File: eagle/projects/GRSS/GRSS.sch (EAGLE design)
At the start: 24 parts, among them J1 MOL-SL-2-RA, J10 MOL-SL-2-RA, J11 M02PTH, J2 MOL-SL-2-RA, J3 MOL-SL-2-RA, J4 MOL-SL-2-RA, J5 MOL-SL-2-RA, J6 MOL-SL-2-RA, J7 MOL-SL-2-RA, J8 MOL-SL-2-RA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

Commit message: modified 555 Timer -> T=~3s
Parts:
- R4: value 76.8k -> 240k; device grss:RES_76R8_0603 -> grss:RES_240R0_0603
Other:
- note added: "555 Timer - ~3s"
- note removed: "555 Timer - ~1Hz"
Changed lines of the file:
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@@
 <part name="R2" library="grss" deviceset="RES" device="_0603" technology="_100R" value="100"/>
 <part name="R3" library="grss" deviceset="RES" device="_0603" technology="_100R" value="100"/>
-<part name="R4" library="grss" deviceset="RES" device="_0603" technology="_76R8" value="76.8k"/>
+<part name="R4" library="grss" deviceset="RES" device="_0603" technology="_240R0" value="240k"/>
 <part name="C1" library="grss" deviceset="CAP" device="_0603" technology="_100NF0" value="100nF"/>
 <part name="C2" library="grss" deviceset="CAP" device="_0603" technology="_10UF0" value="10uF"/>
@@
 <sheet>
 <plain>
-<text x="65.786" y="90.17" size="2.54" layer="91">TITLE_TOC</text>
-<text x="65.786" y="85.09" size="2.54" layer="91">BLOCK_DIAGRAM</text>
-<text x="65.786" y="80.01" size="2.54" layer="91">SCHEMATIC</text>
-<text x="22.86" y="154.94" size="6.4516" layer="91">Global Recovery Signalling System (GRSS)</text>
-<text x="191.262" y="12.7" size="2.54" layer="91">TITLE_TOC</text>
+<text x="65.786" y="90.17" size="2.54" layer="95">TITLE_TOC</text>
+<text x="65.786" y="85.09" size="2.54" layer="95">BLOCK_DIAGRAM</text>
+<text x="65.786" y="80.01" size="2.54" layer="95">SCHEMATIC</text>
+<text x="22.86" y="154.94" size="6.4516" layer="95">Global Recovery Signalling System (GRSS)</text>
+<text x="191.262" y="12.7" size="2.54" layer="95">TITLE_TOC</text>
 </plain>
 <instances>
@@
 <sheet>
 <plain>
-<text x="-50.8" y="177.8" size="1.778" layer="91">LED1</text>
-<text x="-50.8" y="157.48" size="1.778" layer="91">LED2</text>
-<text x="-50.8" y="137.16" size="1.778" layer="91">LED3</text>
-<text x="-22.86" y="177.8" size="1.778" layer="91">LED4</text>
-<text x="-22.86" y="157.48" size="1.778" layer="91">LED5</text>
-<text x="-22.86" y="137.16" size="1.778" layer="91">LED6</text>
-<text x="5.08" y="177.8" size="1.778" layer="91">LED7</text>
-<text x="5.08" y="157.48" size="1.778" layer="91">LED8</text>
-<text x="5.08" y="137.16" size="1.778" layer="91">LED9</text>
-<text x="33.02" y="157.48" size="1.778" layer="91">Buzzer</text>
-<text x="-124.46" y="129.54" size="1.778" layer="91">555 Timer - ~1Hz</text>
-<text x="-129.54" y="170.18" size="1.778" layer="91">LDO 9V -&gt; 4.5V</text>
-<text x="21.59" y="68.58" size="2.54" layer="91">SCHEMATIC</text>
+<text x="-50.8" y="177.8" size="1.778" layer="97">LED1</text>
+<text x="-50.8" y="157.48" size="1.778" layer="97">LED2</text>
+<text x="-50.8" y="137.16" size="1.778" layer="97">LED3</text>
+<text x="-22.86" y="177.8" size="1.778" layer="97">LED4</text>
+<text x="-22.86" y="157.48" size="1.778" layer="97">LED5</text>
+<text x="-22.86" y="137.16" size="1.778" layer="97">LED6</text>
+<text x="5.08" y="177.8" size="1.778" layer="97">LED7</text>
+<text x="5.08" y="157.48" size="1.778" layer="97">LED8</text>
+<text x="5.08" y="137.16" size="1.778" layer="97">LED9</text>
+<text x="33.02" y="157.48" size="1.778" layer="97">Buzzer</text>
+<text x="-124.46" y="129.54" size="1.778" layer="97">555 Timer - ~3s</text>
+<text x="-129.54" y="170.18" size="1.778" layer="97">LDO 9V -&gt; 4.5V</text>
+<text x="21.59" y="68.58" size="2.54" layer="95">SCHEMATIC</text>
 </plain>
 <instances>

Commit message: Added NC (no connect) to lib and sch
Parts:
- added NC1: NC, grss:NO_CONNECT
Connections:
- new net N$1: NC1.NC, U2.CVOLT
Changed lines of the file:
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@@
 <part name="FRAME2" library="frames" deviceset="A4L-LOC" device=""/>
 <part name="U$1" library="grss" deviceset="TOC" device="" value="TOC"/>
+<part name="NC1" library="grss" deviceset="NO_CONNECT" device="" value="NC"/>
 </parts>
 <sheets>
@@
 <instance part="J9" gate="G$1" x="17.78" y="137.16"/>
 <instance part="J10" gate="G$1" x="45.72" y="157.48"/>
+<instance part="NC1" gate="G$1" x="-78.74" y="127" rot="R180"/>
 </instances>
 <busses>
@@
 </segment>
 </net>
+<net name="N$1" class="0">
+<segment>
+<pinref part="U2" gate="A" pin="CVOLT"/>
+<pinref part="NC1" gate="G$1" pin="NC"/>
+<wire x1="-78.74" y1="127" x2="-83.82" y2="127" width="0.1524" layer="91"/>
+</segment>
+</net>

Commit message: Package updates for component check / added block diagram sheet
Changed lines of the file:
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@@
 <layers>
 <layer number="1" name="Top" color="4" fill="1" visible="no" active="no"/>
+<layer number="2" name="Route2" color="1" fill="3" visible="no" active="no"/>
+<layer number="3" name="Route3" color="4" fill="3" visible="no" active="no"/>
+<layer number="14" name="Route14" color="1" fill="6" visible="no" active="no"/>
+<layer number="15" name="Route15" color="4" fill="6" visible="no" active="no"/>
 <layer number="16" name="Bottom" color="1" fill="1" visible="no" active="no"/>
 <layer number="17" name="Pads" color="2" fill="1" visible="no" active="no"/>
@@
 <part name="U$1" library="grss" deviceset="TOC" device="" value="TOC"/>
 <part name="NC1" library="grss" deviceset="NO_CONNECT" device="" value="NC"/>
+<part name="FRAME3" library="frames" deviceset="A4L-LOC" device=""/>
 </parts>
 <sheets>
@@
 </instances>
 <busses>
+</busses>
+<nets>
+</nets>
+</sheet>
+<sheet>
+<plain>
+<text x="196.85" y="25.4" size="2.54" layer="91">BLOCK_DIAGRAM</text>
+</plain>
+<instances>
+<instance part="FRAME3" gate="G$1" x="-20.32" y="5.08"/>
+</instances>
+<busses>

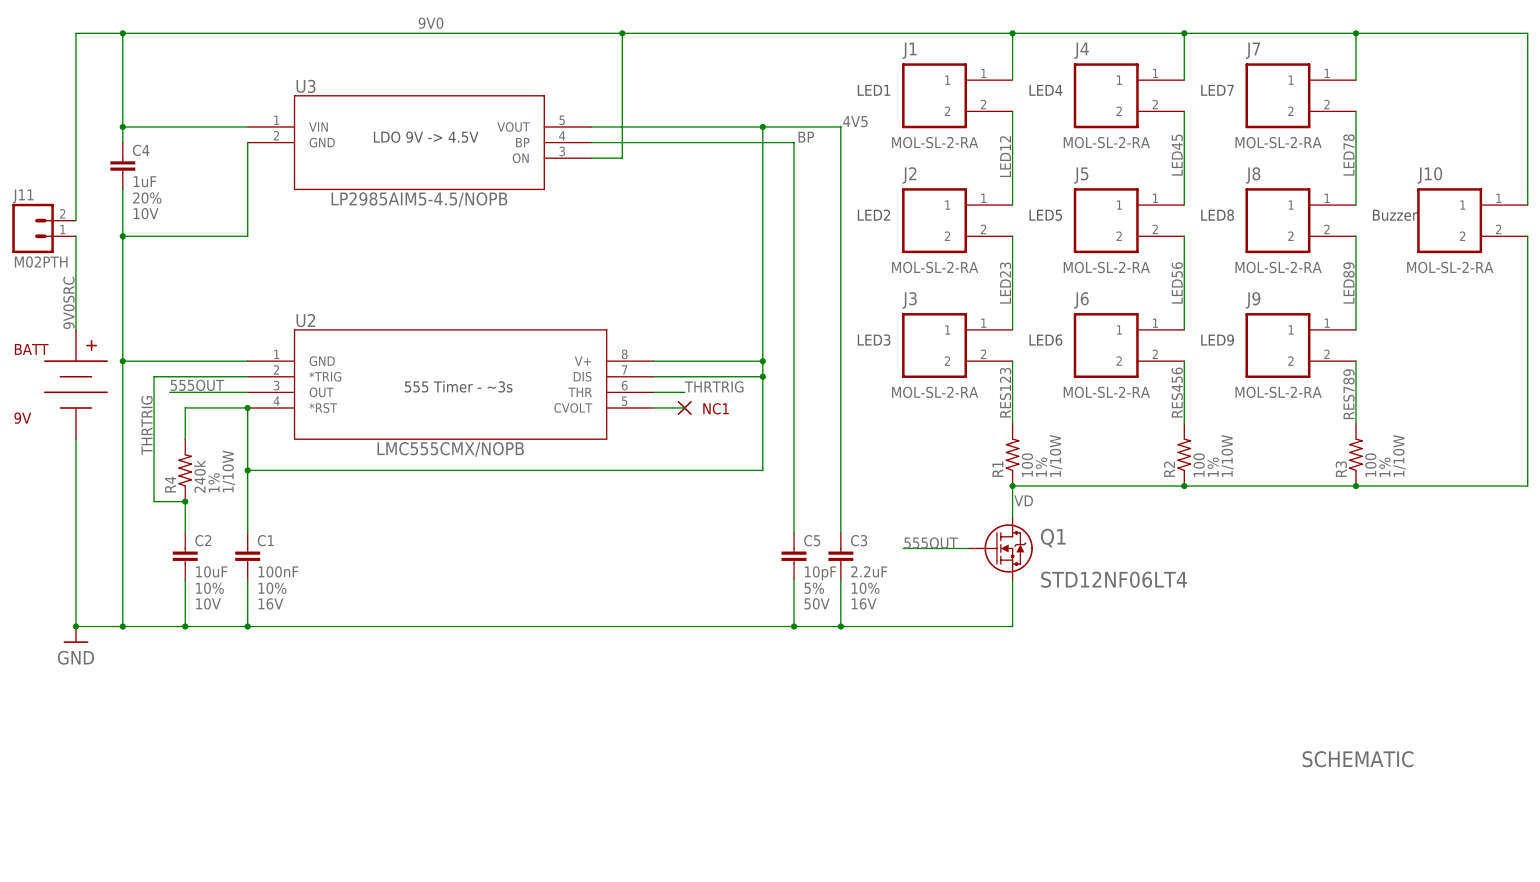
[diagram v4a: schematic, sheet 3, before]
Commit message: Added Test points / updated desc on 555 Timer
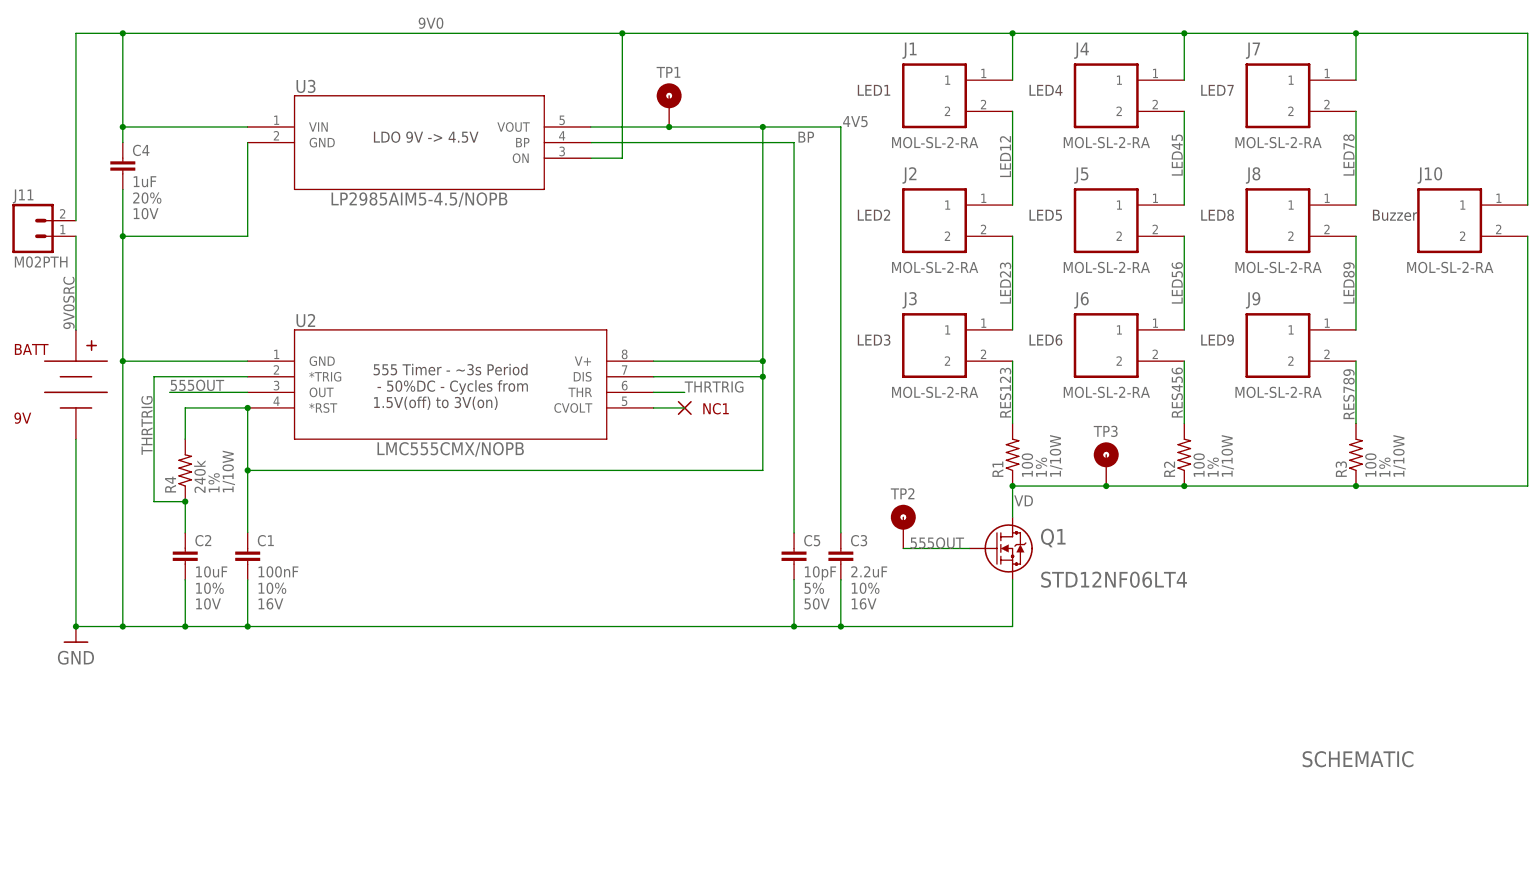
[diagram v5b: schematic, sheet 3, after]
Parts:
- added TP1, TP2, TP3: (no value), grss:TEST_POINT_TP10R_SMD_10R_SMD
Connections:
- net 4V5: now also TP1.TP
- net 555OUT: now also TP2.TP
- net VD: now also TP3.TP
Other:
- note added: "555 Timer - ~3s Period - 50%DC - Cycles from 1.5V(off) to 3V(on)"
- note removed: "555 Timer - ~3s"
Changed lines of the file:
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@@
 <part name="FRAME3" library="frames" deviceset="A4L-LOC" device=""/>
 <part name="U$2" library="grss" deviceset="BLOCK_DIAGRAM" device=""/>
+<part name="TP1" library="grss" deviceset="TEST_POINT" device="_10R_SMD" technology="_TP10R_SMD"/>
+<part name="TP2" library="grss" deviceset="TEST_POINT" device="_10R_SMD" technology="_TP10R_SMD"/>
+<part name="TP3" library="grss" deviceset="TEST_POINT" device="_10R_SMD" technology="_TP10R_SMD"/>
 </parts>
 <sheets>
@@
 <text x="5.08" y="137.16" size="1.778" layer="97">LED9</text>
 <text x="33.02" y="157.48" size="1.778" layer="97">Buzzer</text>
-<text x="-124.46" y="129.54" size="1.778" layer="97">555 Timer - ~3s</text>
+<text x="-129.54" y="127" size="1.778" layer="97">555 Timer - ~3s Period
+ - 50%DC - Cycles from
+1.5V(off) to 3V(on)</text>
 <text x="-129.54" y="170.18" size="1.778" layer="97">LDO 9V -&gt; 4.5V</text>
 <text x="21.59" y="68.58" size="2.54" layer="95">SCHEMATIC</text>
@@
 <instance part="J10" gate="G$1" x="45.72" y="157.48"/>
 <instance part="NC1" gate="G$1" x="-78.74" y="127" rot="R180"/>
+<instance part="TP1" gate="G$1" x="-81.28" y="177.8"/>
+<instance part="TP2" gate="G$1" x="-43.18" y="109.22"/>
+<instance part="TP3" gate="G$1" x="-10.16" y="119.38"/>
 </instances>
 <busses>
@@
 <segment>
 <pinref part="C3" gate="G$1" pin="1"/>
-<wire x1="-93.98" y1="172.72" x2="-66.04" y2="172.72" width="0.1524" layer="91"/>
+<wire x1="-93.98" y1="172.72" x2="-81.28" y2="172.72" width="0.1524" layer="91"/>
+<wire x1="-81.28" y1="172.72" x2="-66.04" y2="172.72" width="0.1524" layer="91"/>
 <wire x1="-66.04" y1="172.72" x2="-53.34" y2="172.72" width="0.1524" layer="91"/>
 <wire x1="-53.34" y1="172.72" x2="-53.34" y2="106.68" width="0.1524" layer="91"/>
@@
 <pinref part="U2" gate="A" pin="V+"/>
 <pinref part="U3" gate="A" pin="VOUT"/>
+<pinref part="TP1" gate="G$1" pin="TP"/>
+<junction x="-81.28" y="172.72"/>
 </segment>
 </net>
@@
 <segment>
 <wire x1="-32.385" y1="104.14" x2="-43.18" y2="104.14" width="0.1524" layer="91"/>
-<label x="-43.18" y="104.14" size="1.778" layer="95"/>
+<label x="-42.164" y="104.14" size="1.778" layer="95"/>
 <pinref part="Q1" gate="A" pin="1"/>
+<pinref part="TP2" gate="G$1" pin="TP"/>
 </segment>
 </net>
@@
 <pinref part="R2" gate="G$1" pin="1"/>
 <pinref part="R3" gate="G$1" pin="1"/>
-<wire x1="-25.4" y1="114.3" x2="2.54" y2="114.3" width="0.1524" layer="91"/>
+<wire x1="-25.4" y1="114.3" x2="-10.16" y2="114.3" width="0.1524" layer="91"/>
+<wire x1="-10.16" y1="114.3" x2="2.54" y2="114.3" width="0.1524" layer="91"/>
 <wire x1="2.54" y1="114.3" x2="30.48" y2="114.3" width="0.1524" layer="91"/>
 <wire x1="30.48" y1="114.3" x2="58.42" y2="114.3" width="0.1524" layer="91"/>
@@
 <label x="-25.146" y="110.998" size="1.778" layer="95"/>
 <pinref part="J10" gate="G$1" pin="2"/>
+<pinref part="TP3" gate="G$1" pin="TP"/>
+<junction x="-10.16" y="114.3"/>
 </segment>
 </net>
@@
 </schematic>
 </drawing>
+<compatibility>
+<note version="6.3" minversion="6.2.2" severity="warning">
+Since Version 6.2.2 text objects can contain more than one line,
+which will not be processed correctly with this version.
+</note>
+</compatibility>
 </eagle>

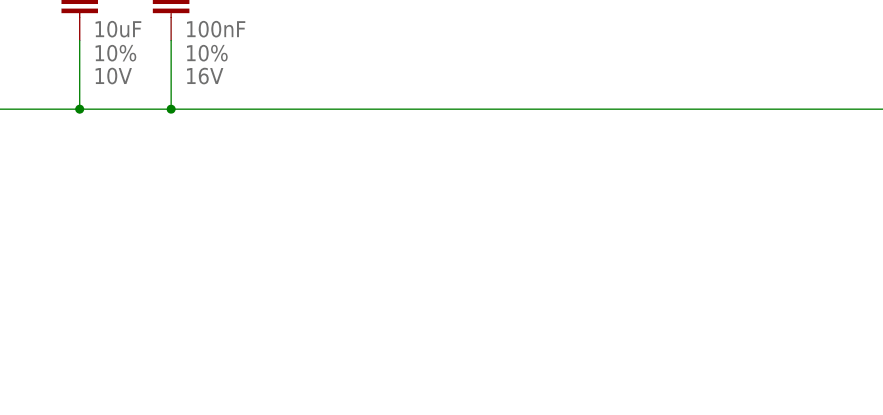
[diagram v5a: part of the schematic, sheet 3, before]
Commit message: added mounting holes to lib / sch
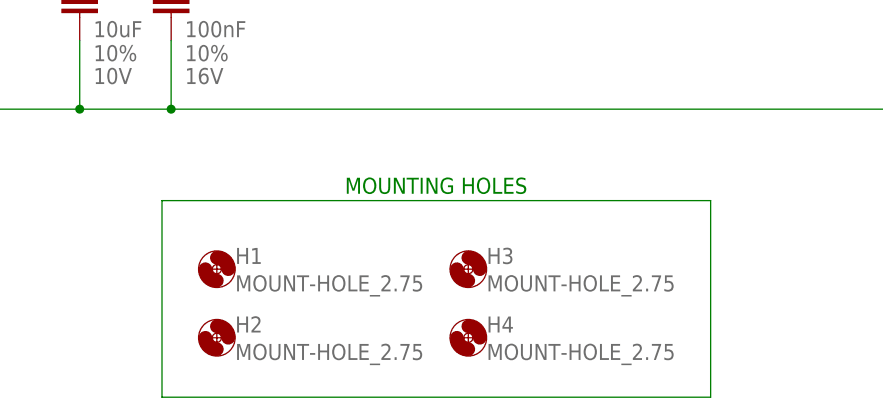
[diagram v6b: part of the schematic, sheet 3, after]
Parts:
- added H1, H2, H3, H4: MOUNT-HOLE_2.75, grss:MOUNT-HOLE_2.75
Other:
- note added: "MOUNTING HOLES"
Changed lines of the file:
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@@
 <part name="TP2" library="grss" deviceset="TEST_POINT" device="_10R_SMD" technology="_TP10R_SMD"/>
 <part name="TP3" library="grss" deviceset="TEST_POINT" device="_10R_SMD" technology="_TP10R_SMD"/>
+<part name="H1" library="grss" deviceset="MOUNT-HOLE" device="_2.75"/>
+<part name="H2" library="grss" deviceset="MOUNT-HOLE" device="_2.75"/>
+<part name="H3" library="grss" deviceset="MOUNT-HOLE" device="_2.75"/>
+<part name="H4" library="grss" deviceset="MOUNT-HOLE" device="_2.75"/>
 </parts>
 <sheets>
@@
 <text x="-129.54" y="170.18" size="1.778" layer="97">LDO 9V -&gt; 4.5V</text>
 <text x="21.59" y="68.58" size="2.54" layer="95">SCHEMATIC</text>
+<text x="-130.556" y="82.042" size="1.778" layer="91">MOUNTING HOLES</text>
 </plain>
 <instances>
@@
 <instance part="TP2" gate="G$1" x="-43.18" y="109.22"/>
 <instance part="TP3" gate="G$1" x="-10.16" y="119.38"/>
+<instance part="H1" gate="G$1" x="-144.78" y="73.66"/>
+<instance part="H2" gate="G$1" x="-144.78" y="66.04"/>
+<instance part="H3" gate="G$1" x="-116.84" y="73.66"/>
+<instance part="H4" gate="G$1" x="-116.84" y="66.04"/>
 </instances>
 <busses>
@@
 </segment>
 </net>
+<net name="N$2" class="0">
+<segment>
+<wire x1="-150.876" y1="81.28" x2="-150.876" y2="59.436" width="0.1524" layer="91"/>
+<wire x1="-150.876" y1="59.436" x2="-89.916" y2="59.436" width="0.1524" layer="91"/>
+<wire x1="-89.916" y1="59.436" x2="-89.916" y2="81.28" width="0.1524" layer="91"/>
+<wire x1="-89.916" y1="81.28" x2="-150.876" y2="81.28" width="0.1524" layer="91"/>
+</segment>
+</net>

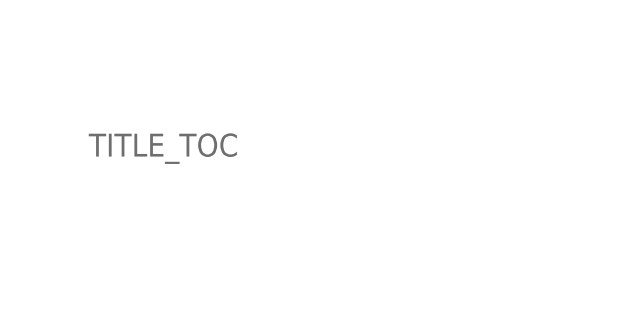
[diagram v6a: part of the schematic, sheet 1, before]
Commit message: Schematic RevA complete. An actual ~block diagram added
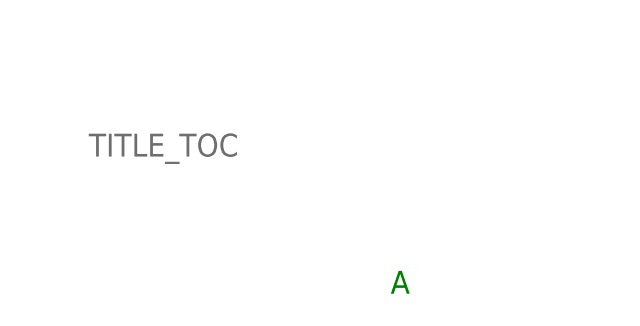
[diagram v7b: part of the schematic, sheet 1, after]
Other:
- note added: "A"
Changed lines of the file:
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@@
 <part name="NC1" library="grss" deviceset="NO_CONNECT" device="" value="NC"/>
 <part name="FRAME3" library="frames" deviceset="A4L-LOC" device=""/>
-<part name="U$2" library="grss" deviceset="BLOCK_DIAGRAM" device=""/>
 <part name="TP1" library="grss" deviceset="TEST_POINT" device="_10R_SMD" technology="_TP10R_SMD"/>
 <part name="TP2" library="grss" deviceset="TEST_POINT" device="_10R_SMD" technology="_TP10R_SMD"/>
@@
 <part name="H3" library="grss" deviceset="MOUNT-HOLE" device="_2.75"/>
 <part name="H4" library="grss" deviceset="MOUNT-HOLE" device="_2.75"/>
+<part name="U$2" library="grss" deviceset="BLOCK_DIAGRAM" device=""/>
 </parts>
 <sheets>
@@
 <text x="22.86" y="154.94" size="6.4516" layer="95">Global Recovery Signalling System (GRSS)</text>
 <text x="191.262" y="12.7" size="2.54" layer="95">TITLE_TOC</text>
+<text x="224.79" y="-2.54" size="2.54" layer="91">A</text>
 </plain>
 <instances>
@@
 <plain>
 <text x="196.85" y="25.4" size="2.54" layer="91">BLOCK_DIAGRAM</text>
+<text x="230.124" y="10.16" size="2.54" layer="91">A</text>
 </plain>
 <instances>
 <instance part="FRAME3" gate="G$1" x="-20.32" y="5.08"/>
-<instance part="U$2" gate="G$1" x="7.62" y="27.94"/>
+<instance part="U$2" gate="G$1" x="0" y="43.18"/>
 </instances>
 <busses>
@@
 <text x="21.59" y="68.58" size="2.54" layer="95">SCHEMATIC</text>
 <text x="-130.556" y="82.042" size="1.778" layer="91">MOUNTING HOLES</text>
+<text x="54.864" y="53.34" size="2.54" layer="91">A</text>
 </plain>
 <instances>
